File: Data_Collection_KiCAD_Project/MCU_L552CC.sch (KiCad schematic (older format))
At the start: 12 parts

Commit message: Fixed Component Libraries
Changed over from project specific to global libraries.
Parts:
- C? (x7): symbol Data_Collection_KiCAD_Project-rescue:C-Device -> Data_Collection_KiCAD_Project-rescue:C-Device-Data_Collection_KiCAD_Project-rescue
- D? (x3): symbol Data_Collection_KiCAD_Project-rescue:LED-Device -> Data_Collection_KiCAD_Project-rescue:LED-Device-Data_Collection_KiCAD_Project-rescue
- U?: symbol Data_Collection_KiCAD_Project-rescue:STM32L031C4Tx-MCU_ST_STM32L0 -> Data_Collection_KiCAD_Project-rescue:STM32L031C4Tx-MCU_ST_STM32L0-Data_Collection_KiCAD_Project-rescue
- Y?: symbol Data_Collection_KiCAD_Project-rescue:Crystal-Device -> Data_Collection_KiCAD_Project-rescue:Crystal-Device-Data_Collection_KiCAD_Project-rescue
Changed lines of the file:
@@
 $Descr A4 11693 8268
 encoding utf-8
-Sheet 5 10
+Sheet 5 9
 Title "STM32L552CC Schematic"
 Date "2021-10-01"
@@
 $EndDescr
 $Comp
-L Data_Collection_KiCAD_Project-rescue:STM32L031C4Tx-MCU_ST_STM32L0 U?
+L Data_Collection_KiCAD_Project-rescue:STM32L031C4Tx-MCU_ST_STM32L0-Data_Collection_KiCAD_Project-rescue U?
 U 1 1 61E9E6C0
 P 8800 4300
@@
 $EndComp
 $Comp
-L Data_Collection_KiCAD_Project-rescue:GND-power #PWR?
+L Data_Collection_KiCAD_Project-rescue:GND-power-Data_Collection_KiCAD_Project-rescue #PWR?
 U 1 1 61E9E6C6
 P 8700 6000
@@
 	8800 5950 8900 5950
 $Comp
-L Data_Collection_KiCAD_Project-rescue:+3.3V-power #PWR?
+L Data_Collection_KiCAD_Project-rescue:+3.3V-power-Data_Collection_KiCAD_Project-rescue #PWR?
 U 1 1 61E9E6D6
 P 9200 2700
@@
 Microcontroller Chip
 $Comp
-L Data_Collection_KiCAD_Project-rescue:GND-power #PWR?
+L Data_Collection_KiCAD_Project-rescue:GND-power-Data_Collection_KiCAD_Project-rescue #PWR?
 U 1 1 61E9E6FD
 P 6700 3300
@@
 NoConn ~ 9400 4200
 $Comp
-L Data_Collection_KiCAD_Project-rescue:LED-Device D?
+L Data_Collection_KiCAD_Project-rescue:LED-Device-Data_Collection_KiCAD_Project-rescue D?
 U 1 1 61E9E710
 P 9950 5300
@@
 $EndComp
 $Comp
-L Data_Collection_KiCAD_Project-rescue:LED-Device D?
+L Data_Collection_KiCAD_Project-rescue:LED-Device-Data_Collection_KiCAD_Project-rescue D?
 U 1 1 61E9E716
 P 10300 5300
@@
 $EndComp
 $Comp
-L Data_Collection_KiCAD_Project-rescue:LED-Device D?
+L Data_Collection_KiCAD_Project-rescue:LED-Device-Data_Collection_KiCAD_Project-rescue D?
 U 1 1 61E9E71C
 P 10650 5300
@@
 	9950 5000 9400 5000
 $Comp
-L Data_Collection_KiCAD_Project-rescue:GND-power #PWR?
+L Data_Collection_KiCAD_Project-rescue:GND-power-Data_Collection_KiCAD_Project-rescue #PWR?
 U 1 1 61E9E724
 P 9950 5450
@@
 $EndComp
 $Comp
-L Data_Collection_KiCAD_Project-rescue:GND-power #PWR?
+L Data_Collection_KiCAD_Project-rescue:GND-power-Data_Collection_KiCAD_Project-rescue #PWR?
 U 1 1 61E9E72A
 P 10300 5450
@@
 $EndComp
 $Comp
-L Data_Collection_KiCAD_Project-rescue:GND-power #PWR?
+L Data_Collection_KiCAD_Project-rescue:GND-power-Data_Collection_KiCAD_Project-rescue #PWR?
 U 1 1 61E9E730
 P 10650 5450
@@
 CL = 2 * (Cload - Cstray)\nCstray ≈ 20pF, Cstray ≈ 5pF\nCL = 2 * (Cload - 5pF)\nCL = 30pF
 $Comp
-L Data_Collection_KiCAD_Project-rescue:Crystal-Device Y?
+L Data_Collection_KiCAD_Project-rescue:Crystal-Device-Data_Collection_KiCAD_Project-rescue Y?
 U 1 1 61E9E73C
 P 7100 4300
@@
 $EndComp
 $Comp
-L Data_Collection_KiCAD_Project-rescue:C-Device C?
+L Data_Collection_KiCAD_Project-rescue:C-Device-Data_Collection_KiCAD_Project-rescue C?
 U 1 1 61E9E742
 P 6850 4650
@@
 $EndComp
 $Comp
-L Data_Collection_KiCAD_Project-rescue:C-Device C?
+L Data_Collection_KiCAD_Project-rescue:C-Device-Data_Collection_KiCAD_Project-rescue C?
 U 1 1 61E9E748
 P 7350 4650
@@
 	7350 4300 7250 4300
 $Comp
-L Data_Collection_KiCAD_Project-rescue:GND-power #PWR?
+L Data_Collection_KiCAD_Project-rescue:GND-power-Data_Collection_KiCAD_Project-rescue #PWR?
 U 1 1 61E9E750
 P 6850 4800
@@
 $EndComp
 $Comp
-L Data_Collection_KiCAD_Project-rescue:GND-power #PWR?
+L Data_Collection_KiCAD_Project-rescue:GND-power-Data_Collection_KiCAD_Project-rescue #PWR?
 U 1 1 61E9E756
 P 7350 4800
@@
 	6850 3400 6850 4300
 $Comp
-L Data_Collection_KiCAD_Project-rescue:GND-power #PWR?
+L Data_Collection_KiCAD_Project-rescue:GND-power-Data_Collection_KiCAD_Project-rescue #PWR?
 U 1 1 61EA2645
 P 900 1700
@@
 $EndComp
 $Comp
-L Data_Collection_KiCAD_Project-rescue:C-Device C?
+L Data_Collection_KiCAD_Project-rescue:C-Device-Data_Collection_KiCAD_Project-rescue C?
 U 1 1 61EA264B
 P 900 1450
@@
 $EndComp
 $Comp
-L Data_Collection_KiCAD_Project-rescue:+3.3V-power #PWR?
+L Data_Collection_KiCAD_Project-rescue:+3.3V-power-Data_Collection_KiCAD_Project-rescue #PWR?
 U 1 1 61EA2651
 P 900 1200
@@
 	900  1200 900  1250
 $Comp
-L Data_Collection_KiCAD_Project-rescue:C-Device C?
+L Data_Collection_KiCAD_Project-rescue:C-Device-Data_Collection_KiCAD_Project-rescue C?
 U 1 1 61EA2659
 P 1300 1450
@@
 $EndComp
 $Comp
-L Data_Collection_KiCAD_Project-rescue:C-Device C?
+L Data_Collection_KiCAD_Project-rescue:C-Device-Data_Collection_KiCAD_Project-rescue C?
 U 1 1 61EA265F
 P 1750 1450
@@
 $EndComp
 $Comp
-L Data_Collection_KiCAD_Project-rescue:C-Device C?
+L Data_Collection_KiCAD_Project-rescue:C-Device-Data_Collection_KiCAD_Project-rescue C?
 U 1 1 61EA2665
 P 2200 1450
@@
 	1300 1650 1750 1650
 $Comp
-L Data_Collection_KiCAD_Project-rescue:C-Device C?
+L Data_Collection_KiCAD_Project-rescue:C-Device-Data_Collection_KiCAD_Project-rescue C?
 U 1 1 61EA267F
 P 2650 1450

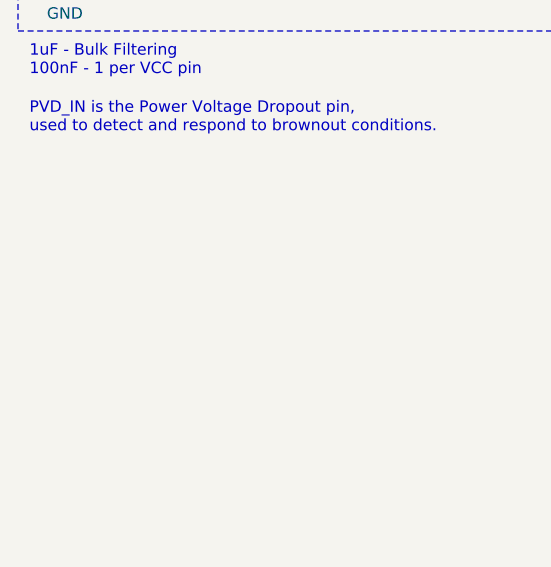
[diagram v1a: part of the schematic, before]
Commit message: i2c Pullups added
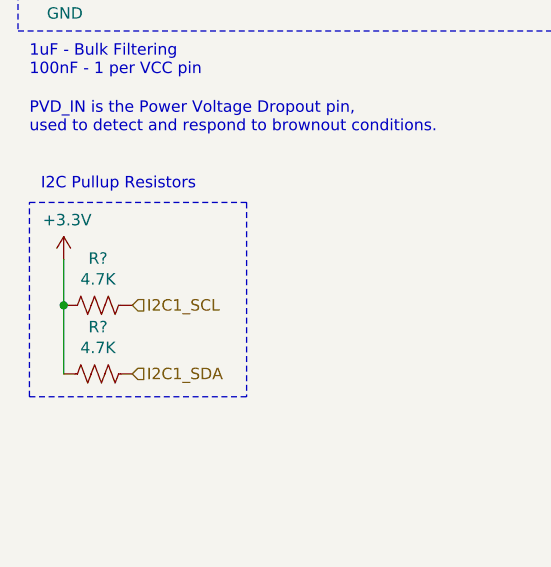
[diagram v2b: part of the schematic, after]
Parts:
- added R? (x2): 4.7K, symbol Device:R_US
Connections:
- net +3V3: now also R?.2, R?.2
- net I2C1_SCL: now also R?.1
- net I2C1_SDA: now also R?.1
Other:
- note added: "I2C Pullup Resistors"
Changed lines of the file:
@@
 Text HLabel 2700 1250 2    50   Output ~ 0
 PVD_IN
+Text HLabel 1200 3450 2    50   Input ~ 0
+I2C1_SDA
+Text HLabel 1200 3150 2    50   Input ~ 0
+I2C1_SCL
+$Comp
+L Device:R_US R?
+U 1 1 619DE947
+P 1050 3150
+F 0 "R?" V 845 3150 50  0000 C CNN
+F 1 "4.7K" V 936 3150 50  0000 C CNN
+F 2 "" V 1090 3140 50  0001 C CNN
+F 3 "~" H 1050 3150 50  0001 C CNN
+	1    1050 3150
+	0    1    1    0
+$EndComp
+$Comp
+L Device:R_US R?
+U 1 1 619DFE15
+P 1050 3450
+F 0 "R?" V 845 3450 50  0000 C CNN
+F 1 "4.7K" V 936 3450 50  0000 C CNN
+F 2 "" V 1090 3440 50  0001 C CNN
+F 3 "~" H 1050 3450 50  0001 C CNN
+	1    1050 3450
+	0    1    1    0
+$EndComp
+Wire Wire Line
+	900  3450 900  3150
+Connection ~ 900  3150
+$Comp
+L Data_Collection_KiCAD_Project-rescue:+3.3V-power-Data_Collection_KiCAD_Project-rescue #PWR?
+U 1 1 619E313D
+P 900 2950
+AR Path="/619E313D" Ref="#PWR?"  Part="1"
+AR Path="/61E8EFE4/619E313D" Ref="#PWR?"  Part="1"
+F 0 "#PWR?" H 900 2800 50  0001 C CNN
+F 1 "+3.3V" H 915 3123 50  0000 C CNN
+F 2 "" H 900 2950 50  0001 C CNN
+F 3 "" H 900 2950 50  0001 C CNN
+	1    900  2950
+	1    0    0    -1
+$EndComp
+Wire Wire Line
+	900  2950 900  3150
+Wire Notes Line
+	750  2700 1700 2700
+Wire Notes Line
+	1700 2700 1700 3550
+Wire Notes Line
+	1700 3550 750  3550
+Wire Notes Line
+	750  3550 750  2700
+Text Notes 800  2650 0    50   ~ 0
+I2C Pullup Resistors
 $EndSCHEMATC

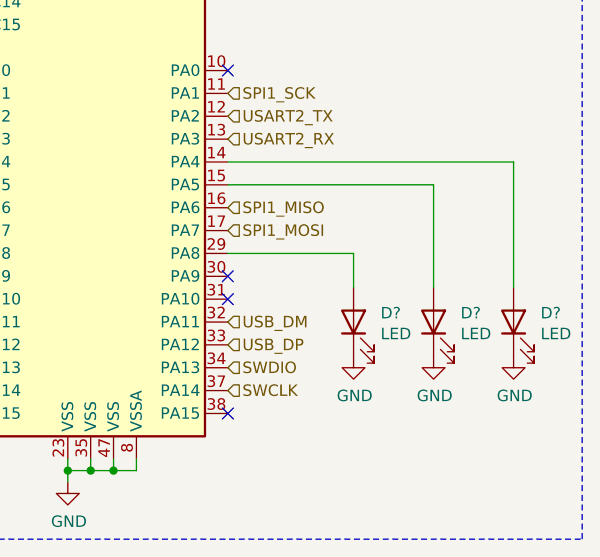
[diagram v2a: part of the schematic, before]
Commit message: Added Resistors for LED
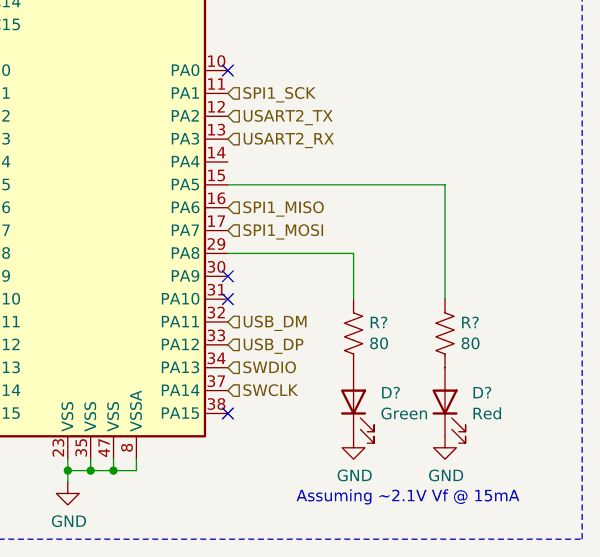
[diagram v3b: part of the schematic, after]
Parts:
- removed D? (x2): LED, symbol Data_Collection_KiCAD_Project-rescue:LED-Device-Data_Collection_KiCAD_Project-r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
- added D?: Red, Diode_SMD:D_0603_1608Metric_Castellated, symbol Data_Collection_KiCAD_Project-rescue:LED-Device-Data_Collection_KiCAD_Project-r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
- added R? (x2): 80, Resistor_SMD:R_0603_1608Metric, symbol Device:R_US
- D?: value LED -> Green; footprint (none) -> Diode_SMD:D_0603_1608Metric_Castellated; Digikey (none) -> https://www.digikey.com/en/products/detail/rohm-semiconduct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
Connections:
- net GND: now also D?.1 (K)
- net at U?.15 (PA5): now also R?.1
- net at U?.29 (PA8): now also R?.1; no longer D?.2 (A)
- new net: D?.2 (A), R?.2 (x2)
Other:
- note added: "Assuming ~~2.1V Vf @ 15mA"
- moved on the sheet: D?
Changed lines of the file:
@@
 L Data_Collection_KiCAD_Project-rescue:LED-Device-Data_Collection_KiCAD_Project-rescue D?
 U 1 1 61E9E710
-P 9950 5300
+P 9950 5650
 AR Path="/61E9E710" Ref="D?"  Part="1"
 AR Path="/61E8EFE4/61E9E710" Ref="D?"  Part="1"
-F 0 "D?" V 9989 5182 50  0000 R CNN
-F 1 "LED" V 9898 5182 50  0000 R CNN
-F 2 "" H 9950 5300 50  0001 C CNN
-F 3 "~" H 9950 5300 50  0001 C CNN
-	1    9950 5300
+F 0 "D?" V 9989 5532 50  0000 R CNN
+F 1 "Green" V 9898 5532 50  0000 R CNN
+F 2 "Diode_SMD:D_0603_1608Metric_Castellated" H 9950 5650 50  0001 C CNN
+F 3 "https://fscdn.rohm.com/en/products/databook/datasheet/opto/led/chip_mono/sml-d12x8_d13x8-e.pdf" H 9950 5650 50  0001 C CNN
+F 4 "https://www.digikey.com/en/products/detail/rohm-semiconductor/SML-D12P8WT86/1641798" V 9950 5650 50  0001 C CNN "Digikey"
+	1    9950 5650
 	0    -1   -1   0
 $EndComp
-$Comp
-L Data_Collection_KiCAD_Project-rescue:LED-Device-Data_Collection_KiCAD_Project-rescue D?
-U 1 1 61E9E716
-P 10300 5300
-AR Path="/61E9E716" Ref="D?"  Part="1"
-AR Path="/61E8EFE4/61E9E716" Ref="D?"  Part="1"
-F 0 "D?" V 10339 5182 50  0000 R CNN
-F 1 "LED" V 10248 5182 50  0000 R CNN
-F 2 "" H 10300 5300 50  0001 C CNN
-F 3 "~" H 10300 5300 50  0001 C CNN
-	1    10300 5300
-	0    -1   -1   0
-$EndComp
-$Comp
-L Data_Collection_KiCAD_Project-rescue:LED-Device-Data_Collection_KiCAD_Project-rescue D?
-U 1 1 61E9E71C
-P 10650 5300
-AR Path="/61E9E71C" Ref="D?"  Part="1"
-AR Path="/61E8EFE4/61E9E71C" Ref="D?"  Part="1"
-F 0 "D?" V 10689 5182 50  0000 R CNN
-F 1 "LED" V 10598 5182 50  0000 R CNN
-F 2 "" H 10650 5300 50  0001 C CNN
-F 3 "~" H 10650 5300 50  0001 C CNN
-	1    10650 5300
-	0    -1   -1   0
-$EndComp
-Wire Wire Line
-	9950 5150 9950 5000
 Wire Wire Line
 	9950 5000 9400 5000
@@
 L Data_Collection_KiCAD_Project-rescue:GND-power-Data_Collection_KiCAD_Project-rescue #PWR?
 U 1 1 61E9E724
-P 9950 5450
+P 9950 5800
 AR Path="/61E9E724" Ref="#PWR?"  Part="1"
 AR Path="/61E8EFE4/61E9E724" Ref="#PWR?"  Part="1"
-F 0 "#PWR?" H 9950 5200 50  0001 C CNN
-F 1 "GND" H 9955 5277 50  0000 C CNN
-F 2 "" H 9950 5450 50  0001 C CNN
-F 3 "" H 9950 5450 50  0001 C CNN
-	1    9950 5450
-	1    0    0    -1
-$EndComp
-$Comp
-L Data_Collection_KiCAD_Project-rescue:GND-power-Data_Collection_KiCAD_Project-rescue #PWR?
-U 1 1 61E9E72A
-P 10300 5450
-AR Path="/61E9E72A" Ref="#PWR?"  Part="1"
-AR Path="/61E8EFE4/61E9E72A" Ref="#PWR?"  Part="1"
-F 0 "#PWR?" H 10300 5200 50  0001 C CNN
-F 1 "GND" H 10305 5277 50  0000 C CNN
-F 2 "" H 10300 5450 50  0001 C CNN
-F 3 "" H 10300 5450 50  0001 C CNN
-	1    10300 5450
-	1    0    0    -1
-$EndComp
-$Comp
-L Data_Collection_KiCAD_Project-rescue:GND-power-Data_Collection_KiCAD_Project-rescue #PWR?
-U 1 1 61E9E730
-P 10650 5450
-AR Path="/61E9E730" Ref="#PWR?"  Part="1"
-AR Path="/61E8EFE4/61E9E730" Ref="#PWR?"  Part="1"
-F 0 "#PWR?" H 10650 5200 50  0001 C CNN
-F 1 "GND" H 10655 5277 50  0000 C CNN
-F 2 "" H 10650 5450 50  0001 C CNN
-F 3 "" H 10650 5450 50  0001 C CNN
-	1    10650 5450
-	1    0    0    -1
-$EndComp
-Wire Wire Line
-	10300 4700 10300 5150
-Wire Wire Line
-	9400 4700 10300 4700
-Wire Wire Line
-	10650 5150 10650 4600
-Wire Wire Line
-	9400 4600 10650 4600
+F 0 "#PWR?" H 9950 5550 50  0001 C CNN
+F 1 "GND" H 9955 5627 50  0000 C CNN
+F 2 "" H 9950 5800 50  0001 C CNN
+F 3 "" H 9950 5800 50  0001 C CNN
+	1    9950 5800
+	1    0    0    -1
+$EndComp
 Wire Notes Line
 	10950 6250 10950 2400
@@
 Text Notes 800  2650 0    50   ~ 0
 I2C Pullup Resistors
+$Comp
+L Device:R_US R?
+U 1 1 619EFD59
+P 9950 5350
+F 0 "R?" H 10018 5396 50  0000 L CNN
+F 1 "80" H 10018 5305 50  0000 L CNN
+F 2 "Resistor_SMD:R_0603_1608Metric" V 9990 5340 50  0001 C CNN
+F 3 "~" H 9950 5350 50  0001 C CNN
+	1    9950 5350
+	1    0    0    -1
+$EndComp
+$Comp
+L Device:R_US R?
+U 1 1 619F2A76
+P 10350 5350
+F 0 "R?" H 10418 5396 50  0000 L CNN
+F 1 "80" H 10418 5305 50  0000 L CNN
+F 2 "Resistor_SMD:R_0603_1608Metric" V 10390 5340 50  0001 C CNN
+F 3 "~" H 10350 5350 50  0001 C CNN
+	1    10350 5350
+	1    0    0    -1
+$EndComp
+$Comp
+L Data_Collection_KiCAD_Project-rescue:LED-Device-Data_Collection_KiCAD_Project-rescue D?
+U 1 1 619F2F50
+P 10350 5650
+AR Path="/619F2F50" Ref="D?"  Part="1"
+AR Path="/61E8EFE4/619F2F50" Ref="D?"  Part="1"
+F 0 "D?" V 10389 5532 50  0000 R CNN
+F 1 "Red" V 10298 5532 50  0000 R CNN
+F 2 "Diode_SMD:D_0603_1608Metric_Castellated" H 10350 5650 50  0001 C CNN
+F 3 "https://fscdn.rohm.com/en/products/databook/datasheet/opto/led/chip_mono/sml-d12x8_d13x8-e.pdf" H 10350 5650 50  0001 C CNN
+F 4 "https://www.digikey.com/en/products/detail/rohm-semiconductor/SML-D12U8WT86/1641799" V 10350 5650 50  0001 C CNN "Digikey"
+	1    10350 5650
+	0    -1   -1   0
+$EndComp
+$Comp
+L Data_Collection_KiCAD_Project-rescue:GND-power-Data_Collection_KiCAD_Project-rescue #PWR?
+U 1 1 619F33E0
+P 10350 5800
+AR Path="/619F33E0" Ref="#PWR?"  Part="1"
+AR Path="/61E8EFE4/619F33E0" Ref="#PWR?"  Part="1"
+F 0 "#PWR?" H 10350 5550 50  0001 C CNN
+F 1 "GND" H 10355 5627 50  0000 C CNN
+F 2 "" H 10350 5800 50  0001 C CNN
+F 3 "" H 10350 5800 50  0001 C CNN
+	1    10350 5800
+	1    0    0    -1
+$EndComp
+Wire Wire Line
+	9400 4700 10350 4700
+Wire Wire Line
+	9950 5000 9950 5200
+Wire Wire Line
+	10350 4700 10350 5200
+Text Notes 9700 6100 0    50   ~ 0
+Assuming ~~2.1V Vf @ 15mA
 $EndSCHEMATC

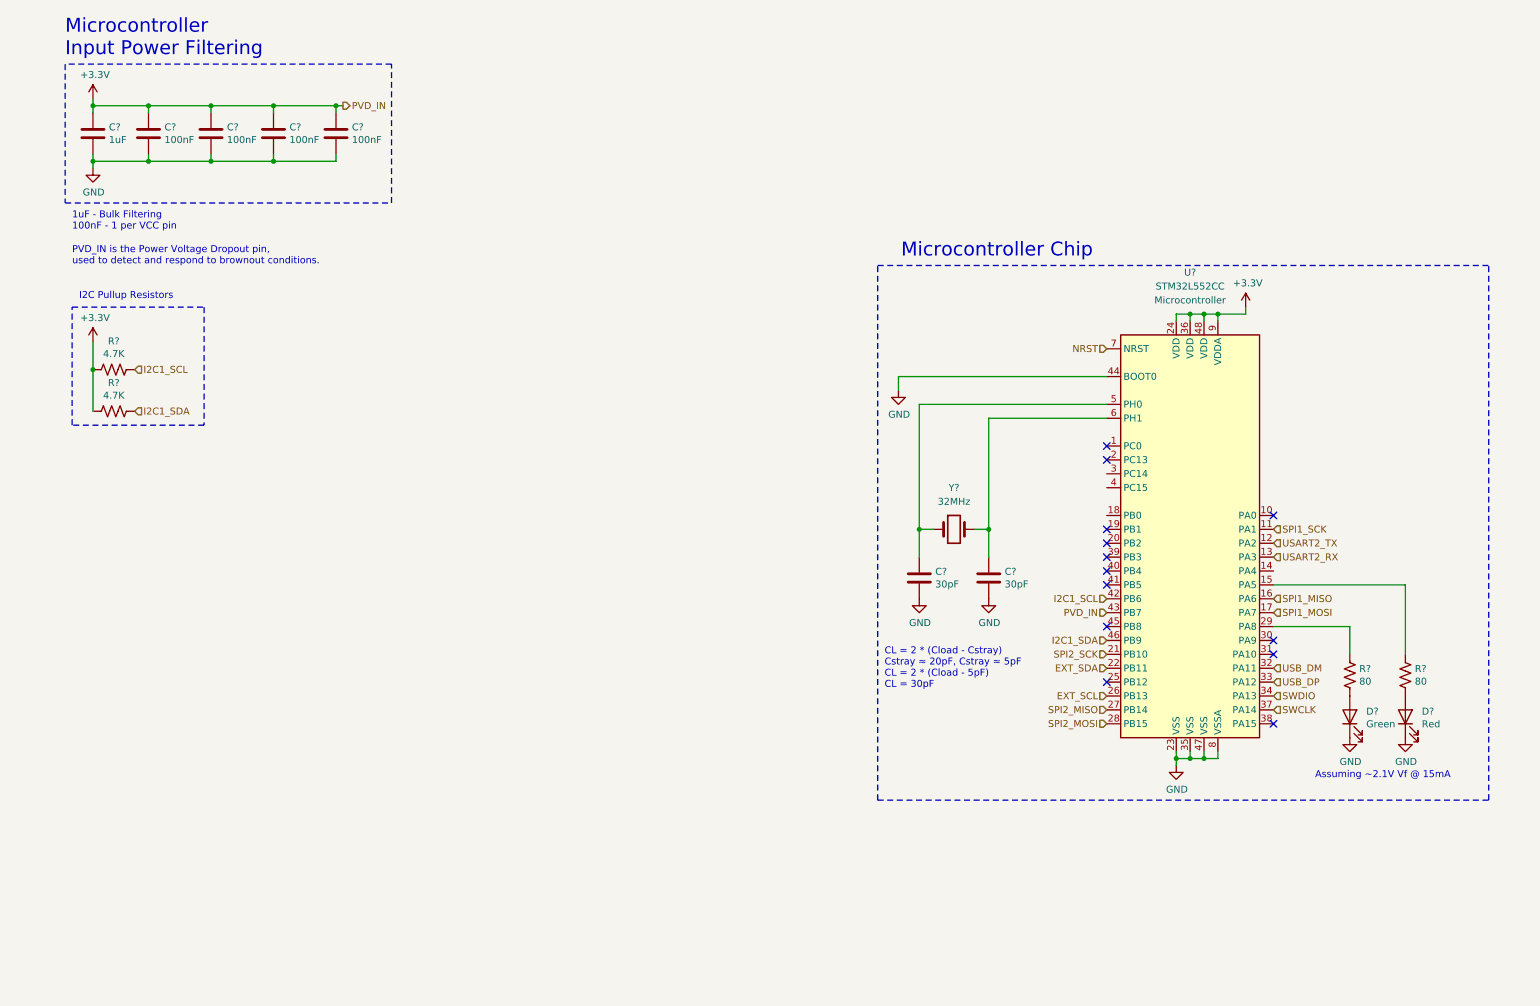
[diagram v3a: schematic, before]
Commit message: footprint and value changes
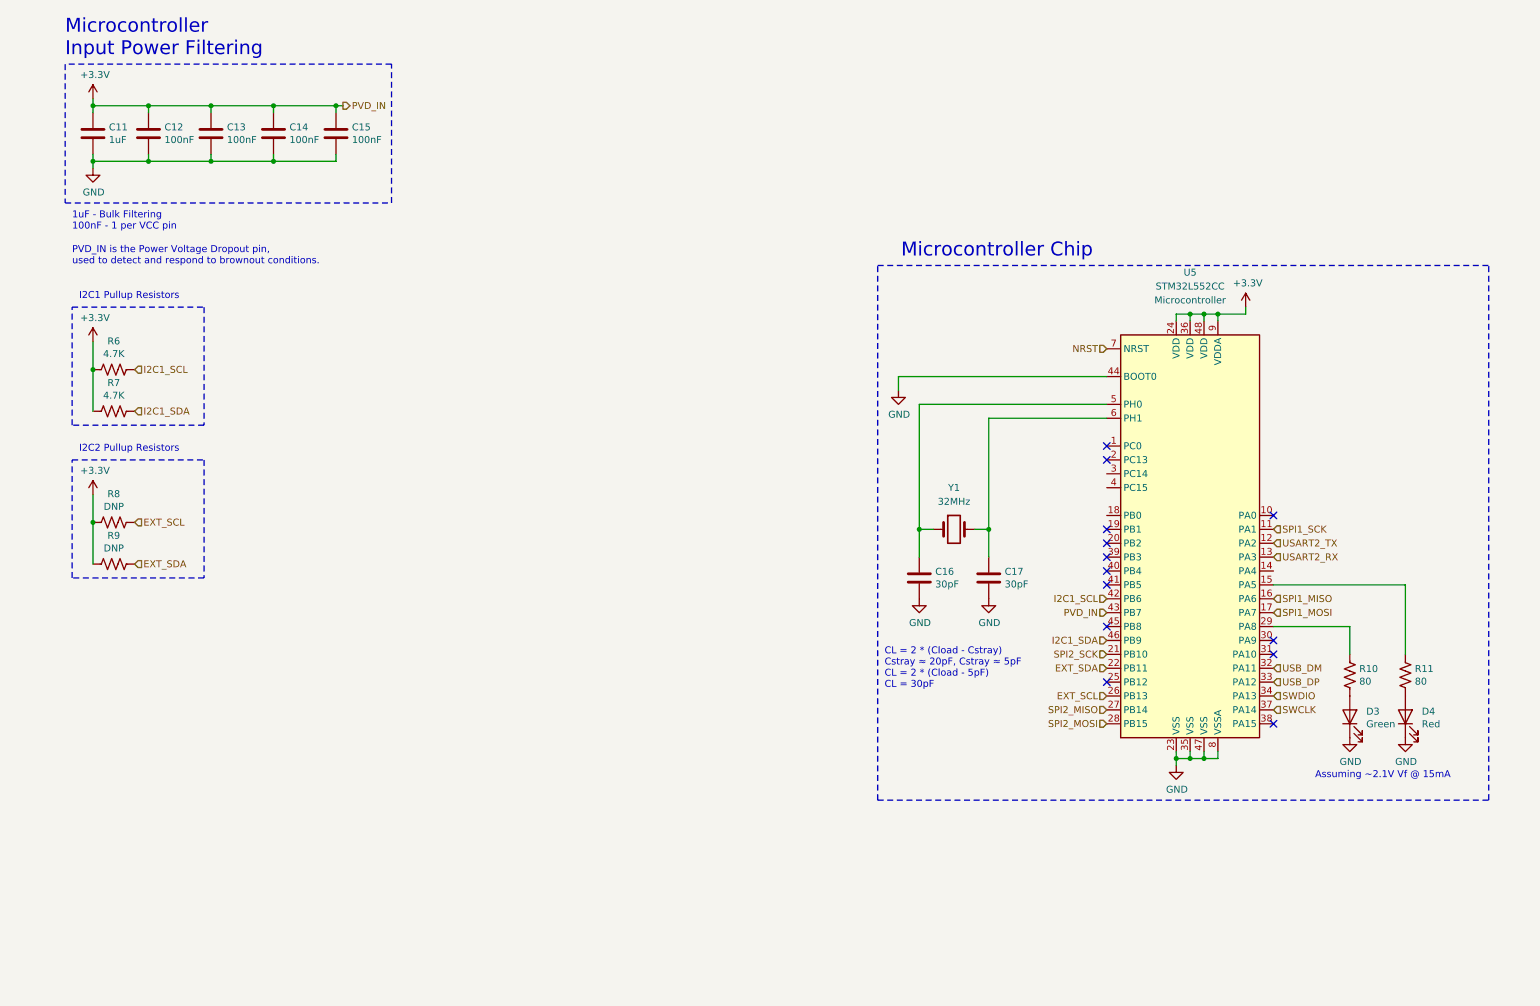
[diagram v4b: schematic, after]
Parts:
- added R8, R9: DNP, Resistor_SMD:R_0603_1608Metric, symbol Device:R_US
- C11, C12, C13, C14, C15, C16, C17: renamed from C?; footprint (none) -> Capacitor_SMD:C_0603_1608Metric
- R6, R7: renamed from R?; footprint (none) -> Resistor_SMD:R_0603_1608Metric
- gave numbers to parts that had none: 6
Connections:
- net +3V3: now also R8.2, R9.2
- net EXT_SCL: now also R8.1
- net EXT_SDA: now also R9.1
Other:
- note added: "I2C1 Pullup Resistors"
- note added: "I2C2 Pullup Resistors"
- note removed: "I2C Pullup Resistors"
